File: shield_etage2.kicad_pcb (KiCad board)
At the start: 2 copper layers, 70.6 x 83.1 mm, 60 parts, among them J1 Conn_01x02, J10 ToF, J11 Moteur, J12 Moteur, J13 butee, J14 Moteur, J15 butee, J16 butee, J18 Conn_01x02, J19 output_CAN, J2 Conn_01x02, J3 ToF, J4 ToF, J5 ToF, J6 ToF, J7 ToF, J8 ToF, J9 ToF, Q1 BSS138, Q2 BSS138, Q3 BSS138, Q4 BSS138, SW1 SW_Push, U1 74HC164, U2 LM317_TO3, U3 LM317_TO3, U4 L293D, U5 L293D, U6 MCP2551-I-P

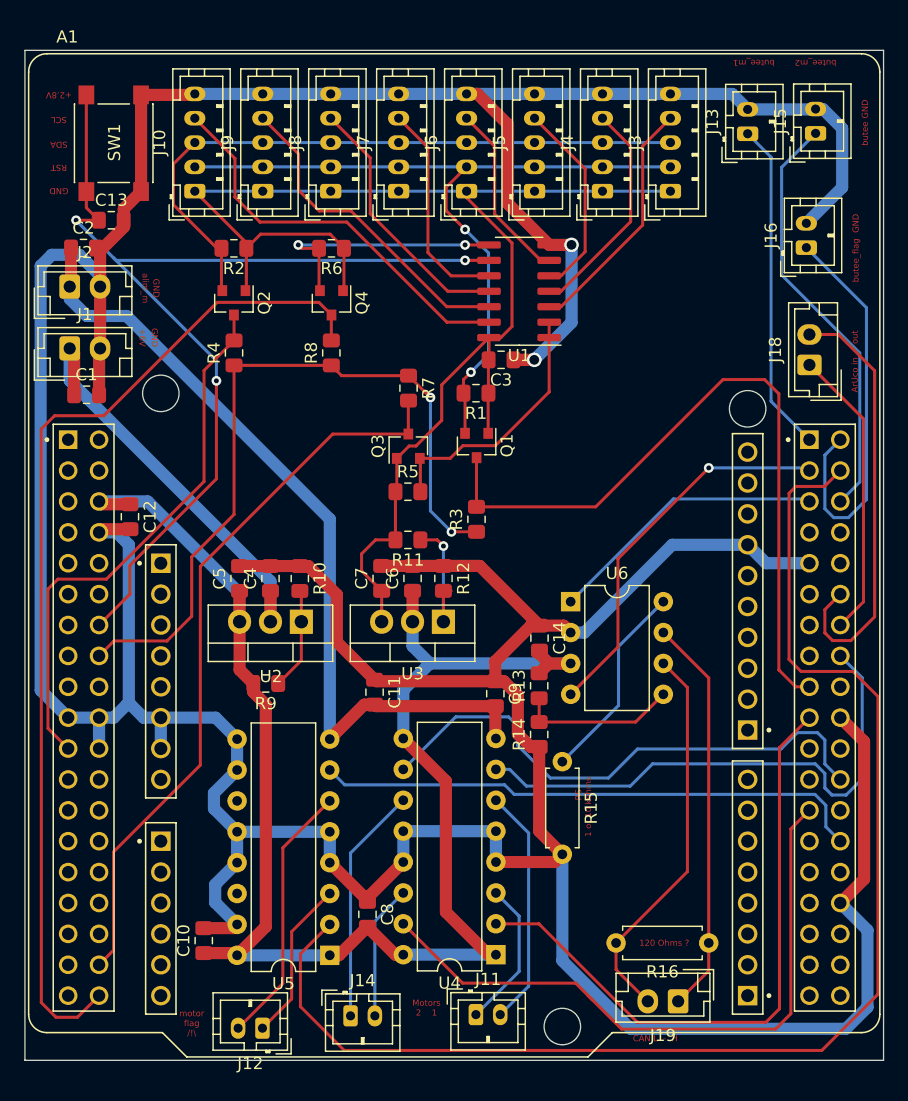
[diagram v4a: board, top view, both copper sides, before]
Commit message: some more changes after Hugo's review, motors connectors not updated
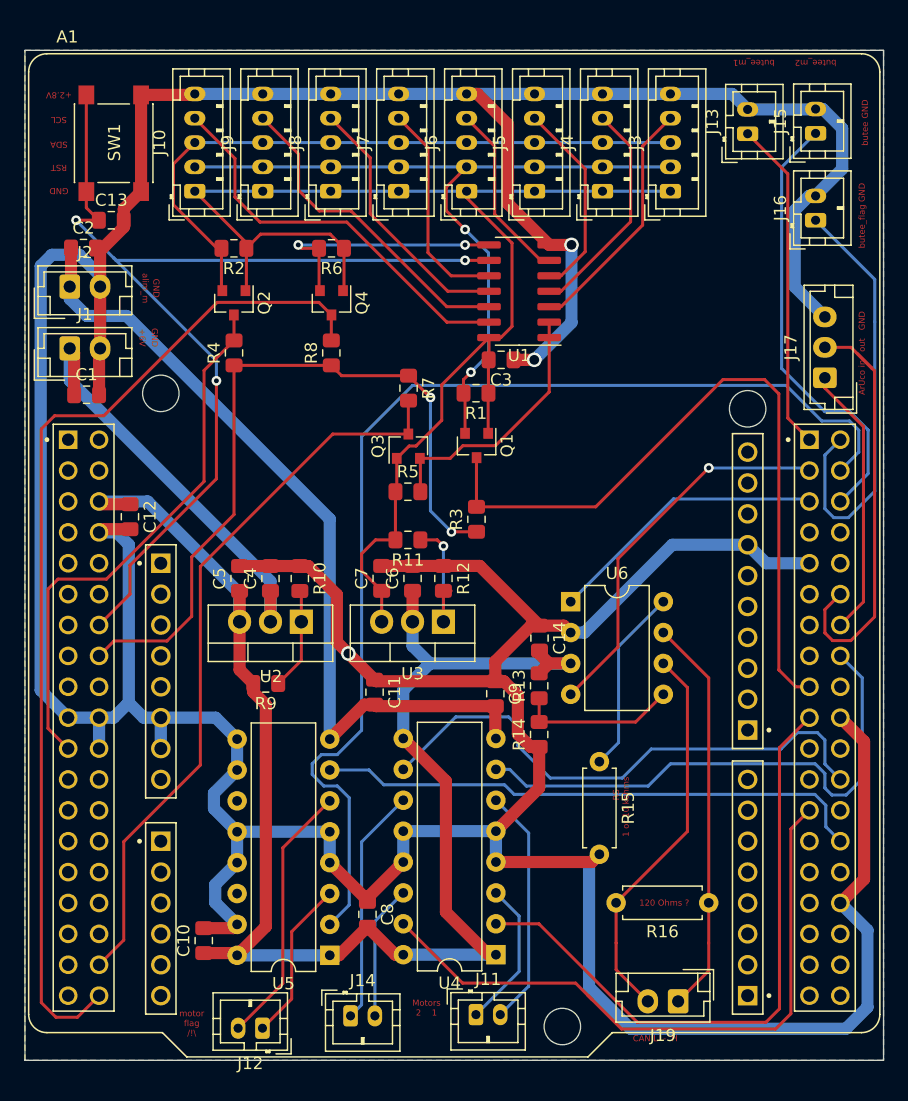
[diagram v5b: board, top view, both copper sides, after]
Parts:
- removed J18: Conn_01x02, Connector_JST:JST_EH_B2B-EH-A_1x02_P2.50mm_Vertical
- added J17: Conn_01x03-Connector_Generic-shield_etage2-rescue, Connector_JST:JST_EH_B3B-EH-A_1x03_P2.50mm_Vertical, F.Cu at (221.7, 99.8)
- moved R16 3.30 mm to (212.2, 143.0)
- moved R15 3.05 mm to (203.2, 131.4)
- moved J16 2.38 mm to (221.0, 86.9)
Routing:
- net /Driver_moteurs/pwm_drapeau: track 110.4 -> 93.3 mm
- net GND: track 423.5 -> 434.2 mm, vias 2 -> 3
- net /FinDeCourse_drapeau/STM32_GPIO: track 33.3 -> 35.8 mm
- net /FinDeCourse_bras2/STM32_GPIO: track 34.8 -> 36.5 mm
- net /ArUco.sch/ArUco1: track 24.0 -> 22.4 mm
- net Net-(R15-Pad1): track 16.6 -> 15.3 mm
- added copper zone on B.Cu, net GND
- added copper zone on F.Cu, net GND
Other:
- net class Power : clearance 0.4 -> 0.35
- board text added: "ArUco in out GND"
- board text removed: "ArUco in out"
